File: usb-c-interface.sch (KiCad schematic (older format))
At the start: 60 parts, among them IC3 TPS7A0518PDBVT, J11 12401598E4_2A, J3 12401598E4_2A, J4 12401598E4_2A, U5 TPS25820DSST, U6 FSUSB30MUX, U7 TXB0104RUT, U8 CBTL02043ABQ,115, U9 FT232RQ-REEL

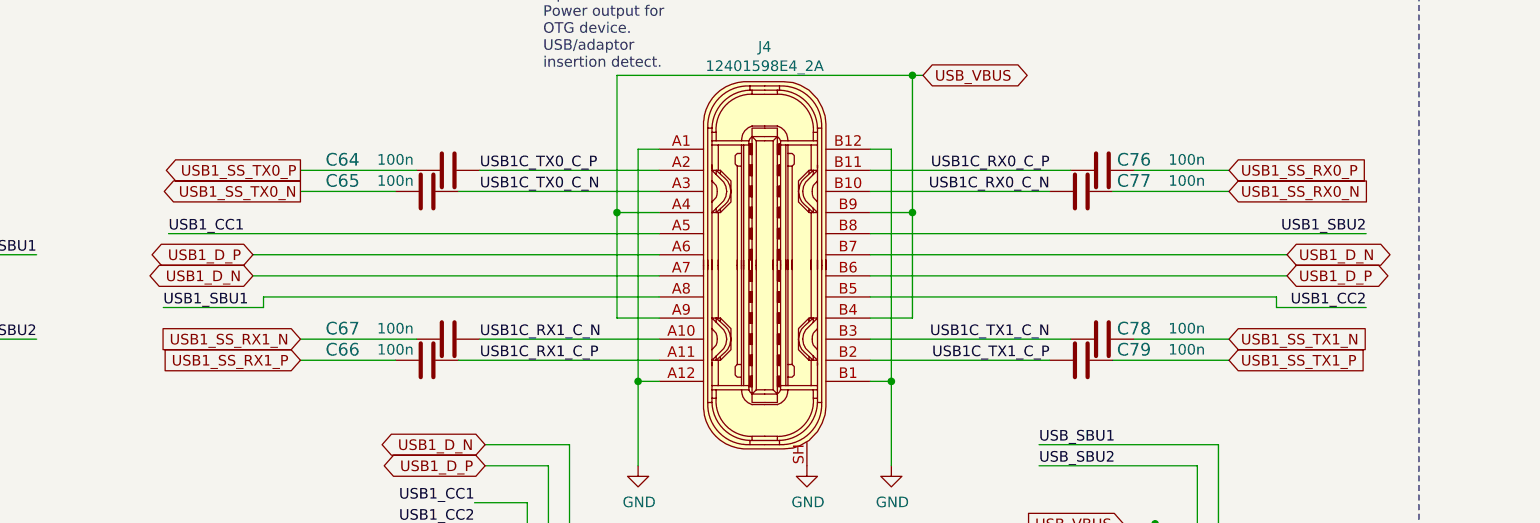
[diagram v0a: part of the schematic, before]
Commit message: Fix connection of CC1 and CC2 signals to som (global and local labels mixed)
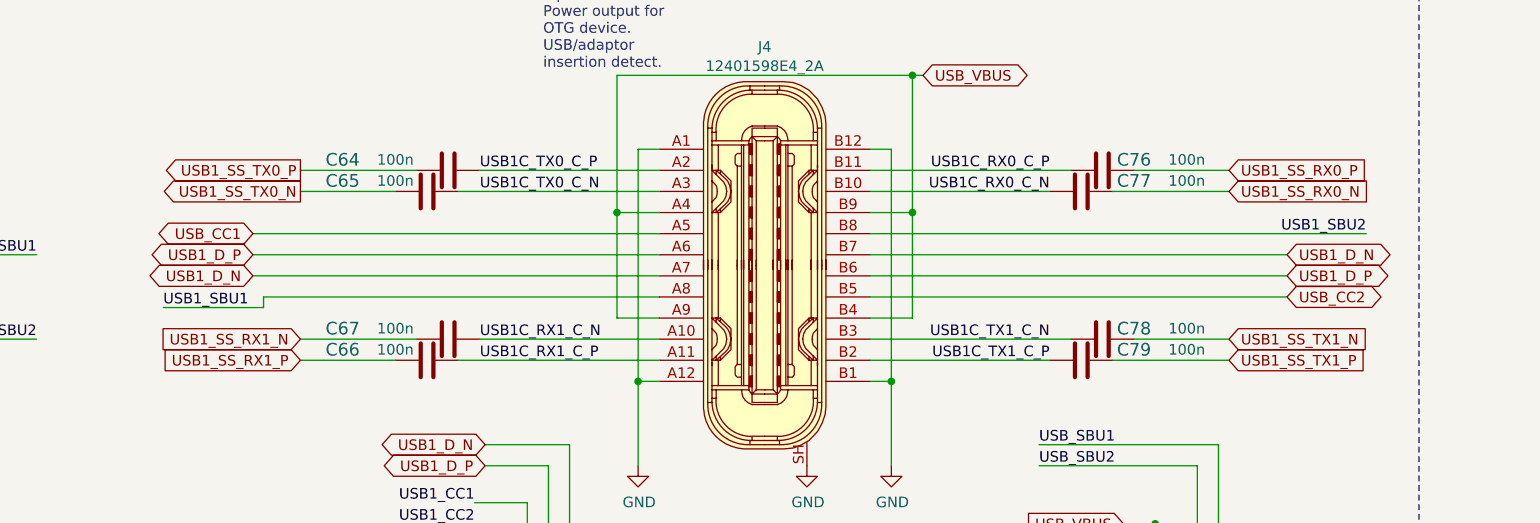
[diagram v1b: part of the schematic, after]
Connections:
- net USB1_CC1: no longer J4.A5
- net USB1_CC2: no longer J4.B5
- new net USB_CC1: J4.A5
- new net USB_CC2: J4.B5
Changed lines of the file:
@@
 Text Label 10950 2225 2    50   ~ 0
 USB1_SBU2
-Text Label 10950 2575 2    50   ~ 0
-USB1_CC2
 Text GLabel 10575 2325 2    50   BiDi ~ 0
 USB1_D_N
@@
 	5250 2575 5725 2575
 Wire Wire Line
-	5275 2225 7600 2225
+	5675 2225 7600 2225
 Wire Wire Line
 	5675 2425 7600 2425
@@
 Text Label 5250 2575 0    50   ~ 0
 USB1_SBU1
-Text Label 5275 2225 0    50   ~ 0
-USB1_CC1
 $Comp
 L sa800u-baseboard-hw:C_100n_0402 C64
@@
 Wire Wire Line
 	8600 2225 10950 2225
-Wire Wire Line
-	10950 2575 10525 2575
-Wire Wire Line
-	10525 2575 10525 2525
-Wire Wire Line
-	10525 2525 8600 2525
 Wire Wire Line
 	9550 2725 8600 2725
@@
 Text GLabel 9350 5750 2    50   Output ~ 0
 USB2_SINK
+Text GLabel 10575 2525 2    50   BiDi ~ 0
+USB_CC2
+Text GLabel 5675 2225 0    50   BiDi ~ 0
+USB_CC1
+Wire Wire Line
+	8600 2525 10575 2525
 $EndSCHEMATC

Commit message: Update labels
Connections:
- net USB_SBU1 is gone; now on net USB1_SBU_P: D9.1 (CH1), D9.10 (CH1)
- net USB_SBU2 is gone; now on net USB1_SBU_P: D9.2 (CH2), D9.9 (CH2)
- net USB1_SBU1 renamed USB1_SBU_N
- net USB1_SBU2 renamed USB1_SBU_P
- net USB_SBU1_2 renamed USB_SBU_NP_P
- net USB_SBU2_1 renamed USB_SBU_NP_N
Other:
- note added: "Note:\nSBU ending with N/P \nto enable routing with \ndifferential tools"
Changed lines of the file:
@@
 $EndComp
 Text Label 10950 2225 2    50   ~ 0
-USB1_SBU2
+USB1_SBU_P
 Text GLabel 10575 2325 2    50   BiDi ~ 0
 USB1_D_N
@@
 Wire Wire Line
 	10050 3600 10050 3775
-Text Label 9400 3325 0    50   ~ 0
-USB_SBU2
 Wire Wire Line
 	9400 3325 10150 3325
@@
 	4175 1575 3900 1575
 Text Label 4650 2325 2    50   ~ 0
-USB1_SBU1
-Text Label 4650 2725 2    50   ~ 0
-USB1_SBU2
-Wire Wire Line
-	4650 2725 4200 2725
+USB1_SBU_N
 Wire Wire Line
 	4650 2325 4200 2325
@@
 	3900 1350 3900 1575
 Connection ~ 3900 1575
-Text Label 3050 2425 2    50   ~ 0
-USB_SBU2_1
-Text Label 3050 2625 2    50   ~ 0
-USB_SBU1_2
+Text Label 3150 2425 2    50   ~ 0
+USB_SBU_NP_N
+Text Label 3150 2625 2    50   ~ 0
+USB_SBU_NP_P
 Text GLabel 2475 2025 0    50   Input ~ 0
 3V3_SYS
@@
 	6350 2825 5900 2825
 Text Label 5250 2575 0    50   ~ 0
-USB1_SBU1
+USB1_SBU_N
 $Comp
 L sa800u-baseboard-hw:C_100n_0402 C64
@@
 	0    1    1    0
 $EndComp
-Text Label 9400 3225 0    50   ~ 0
-USB_SBU1
 $Comp
 L sa800u-baseboard-hw:C_10u_0402 C?
@@
 Wire Wire Line
 	8600 2525 10575 2525
+Text Notes 4100 2650 0    50   ~ 0
+Note:\nSBU ending with N/P \nto enable routing with \ndifferential tools
+Wire Wire Line
+	4650 2725 4200 2725
+Text Label 4650 2725 2    50   ~ 0
+USB1_SBU_P
+Text Label 9400 3225 0    50   ~ 0
+USB1_SBU_P
+Text Label 9400 3325 0    50   ~ 0
+USB1_SBU_P
 $EndSCHEMATC

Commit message: Fix labels
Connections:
- net USB1_CC1 is gone; now on net USB_CC1: D8.4 (CH3), D8.7 (CH3)
- net USB1_CC2 is gone; now on net USB_CC2: D8.5 (CH4), D8.6 (CH4)
- net USB1_SBU_N: now also D9.2 (CH2), D9.9 (CH2)
- net USB1_SBU_P: no longer D9.2 (CH2), D9.9 (CH2)
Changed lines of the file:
@@
 	1    0    0    -1
 $EndComp
-Text Label 6725 3500 2    50   ~ 0
-USB1_CC1
-Text Label 6725 3600 2    50   ~ 0
-USB1_CC2
 Wire Wire Line
 	6725 3600 6875 3600
@@
 USB1_SBU_P
 Text Label 9400 3325 0    50   ~ 0
-USB1_SBU_P
+USB1_SBU_N
+Text GLabel 6725 3500 0    50   BiDi ~ 0
+USB_CC1
+Text GLabel 6725 3600 0    50   BiDi ~ 0
+USB_CC2
 $EndSCHEMATC

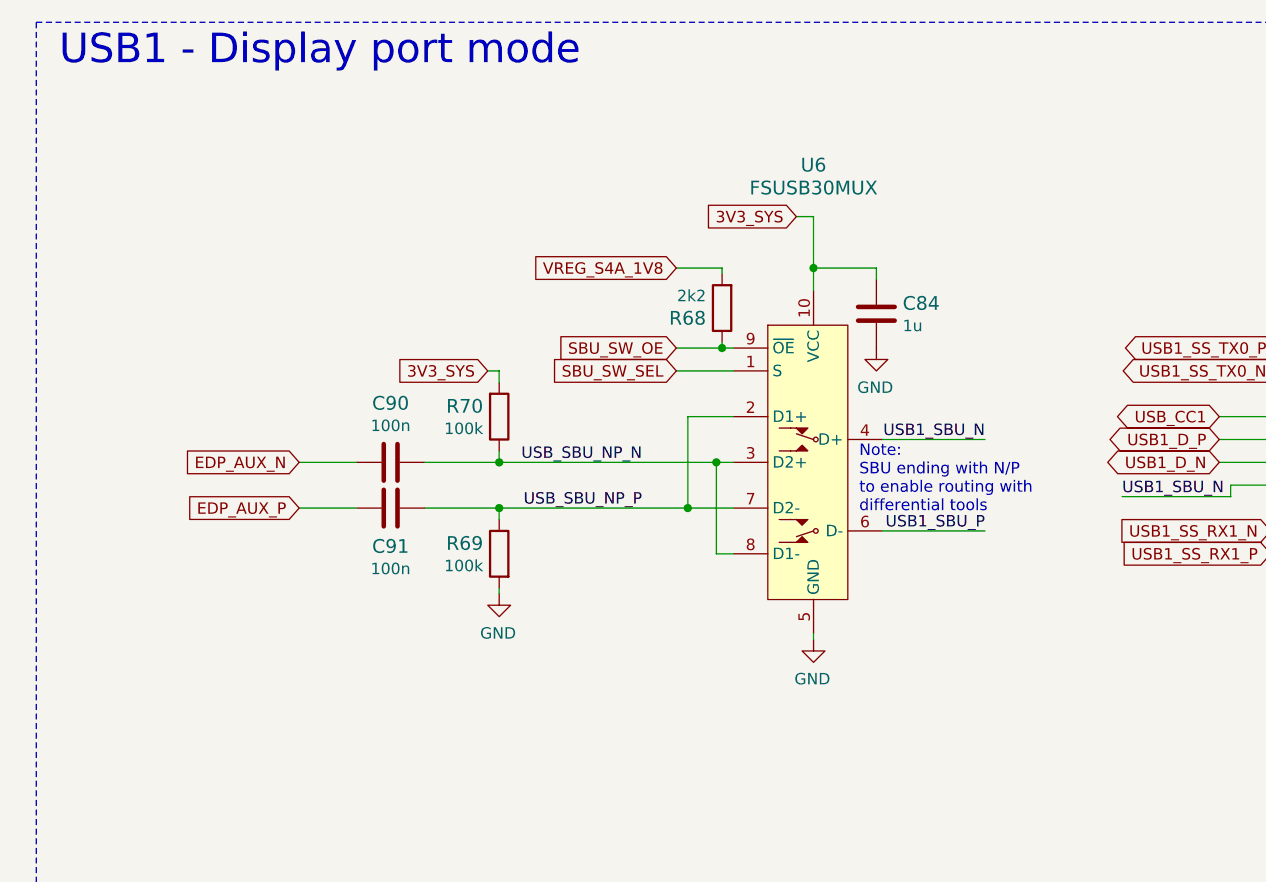
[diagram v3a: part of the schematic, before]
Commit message: Change DP AUX mux
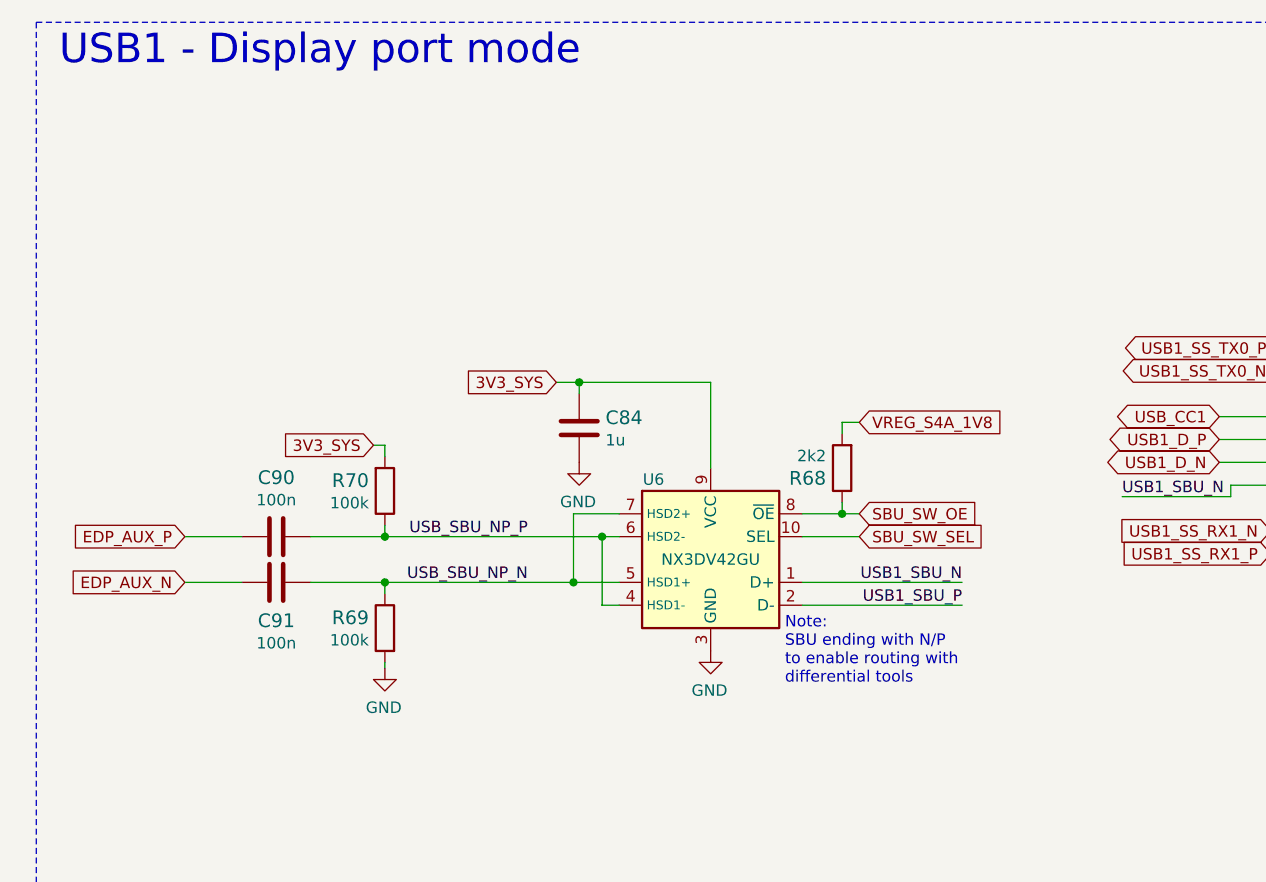
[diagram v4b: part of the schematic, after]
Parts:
- removed U6: FSUSB30MUX, sa800u-baseboard-hw-footprints:MSOP-10_W3mm, symbol sa800u-baseboard-hw:FSUSB30MUX
- added U6: NX3DV42GU, sa800u-baseboard-hw-footprints:XQFN10-1.5x1.9mm, symbol sa800u-baseboard-hw:NX3DV42GU
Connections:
- net 3V3_SYS: now also U6.9 (VCC)
- net EDP_AUX_N: now also C91.1; no longer C90.1
- net EDP_AUX_P: now also C90.1; no longer C91.1
- net GND: now also U6.3 (GND)
- net SBU_SW_OE: now also U6.8 (~OE)
- net SBU_SW_SEL: now also U6.10 (SEL)
- net USB1_SBU_N: now also U6.1 (D+)
- net USB1_SBU_P: now also U6.2 (D-)
- net USB_SBU_NP_N: now also C91.2, R69.1, U6.5 (HSD1+), U6.7 (HSD2+); no longer C90.2, R70.1
- net USB_SBU_NP_P: now also C90.2, R70.1, U6.4 (HSD1-), U6.6 (HSD2-); no longer C91.2, R69.1
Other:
- moved on the sheet: C84, C90, C91, R68, R69, R70

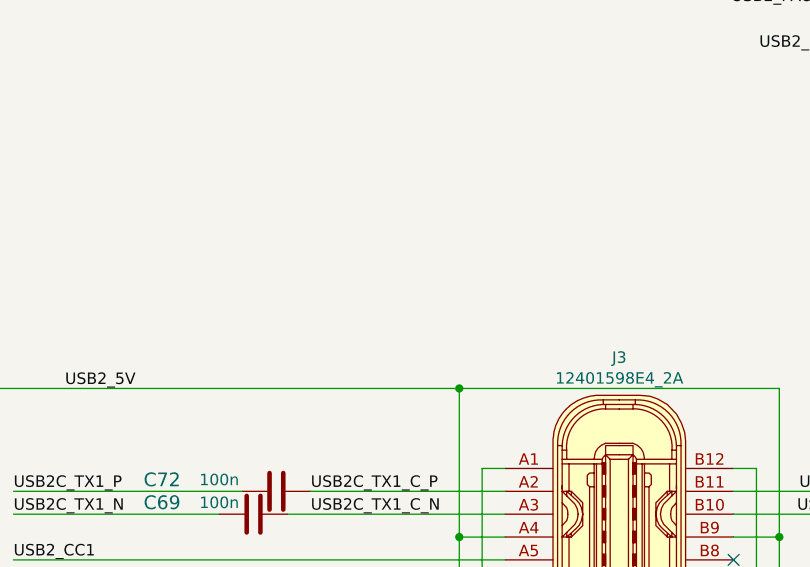
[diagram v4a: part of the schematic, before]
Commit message: Add 47uF caps to USB2C_5V
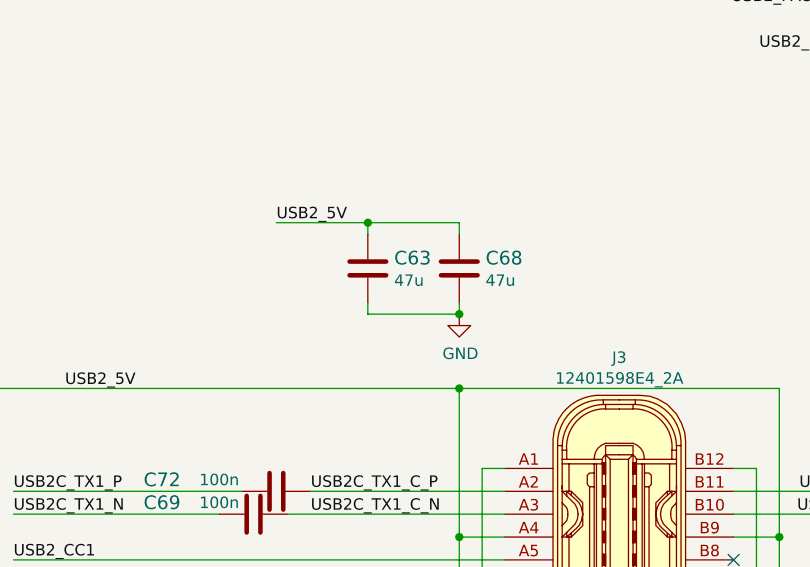
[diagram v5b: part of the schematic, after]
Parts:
- added C63, C68: C_47u_0603, sa800u-baseboard-hw-footprints:0603-cap, symbol sa800u-baseboard-hw:C_47u_0603
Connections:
- net GND: now also C63.2, C68.2
- net USB2_5V: now also C63.1, C68.1
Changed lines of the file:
@@
 Wire Wire Line
 	9625 9575 10325 9575
-Text Label 3000 9950 2    50   ~ 0
-USB2C_TX2_N
-Text Label 3000 9850 2    50   ~ 0
-USB2C_TX2_P
-Text Label 3000 10250 2    50   ~ 0
-USB2C_RX2_N
-Text Label 3000 10150 2    50   ~ 0
-USB2C_RX2_P
-Wire Wire Line
-	2450 9950 3000 9950
-Wire Wire Line
-	2450 9850 3000 9850
-Wire Wire Line
-	2450 10250 3000 10250
-Wire Wire Line
-	2450 10150 3000 10150
-Text Label 3000 9150 2    50   ~ 0
-USB2C_TX1_N
-Text Label 3000 9050 2    50   ~ 0
-USB2C_TX1_P
-Text Label 3000 9450 2    50   ~ 0
-USB2C_RX1_N
-Text Label 3000 9350 2    50   ~ 0
-USB2C_RX1_P
-Wire Wire Line
-	2450 9150 3000 9150
-Wire Wire Line
-	2450 9050 3000 9050
-Wire Wire Line
-	2450 9450 3000 9450
-Wire Wire Line
-	2450 9350 3000 9350
-Text GLabel 1150 9550 0    50   Input ~ 0
-USB2_SS_RX_P
-Text GLabel 1150 9650 0    50   Input ~ 0
-USB2_SS_RX_N
-Text GLabel 1150 9250 0    50   Output ~ 0
-USB2_SS_TX_P
-Text GLabel 1150 9350 0    50   Output ~ 0
-USB2_SS_TX_N
 Wire Wire Line
 	13800 8000 14125 8000
@@
 Wire Wire Line
 	2875 2075 3450 2075
+Text Label 3000 10250 2    50   ~ 0
+USB2C_RX2_N
+Text Label 3000 10150 2    50   ~ 0
+USB2C_RX2_P
+Wire Wire Line
+	2450 10250 3000 10250
+Wire Wire Line
+	2450 10150 3000 10150
+Wire Wire Line
+	2450 9850 3000 9850
+Wire Wire Line
+	2450 9950 3000 9950
+Text Label 3000 9850 2    50   ~ 0
+USB2C_TX2_P
+Text Label 3000 9950 2    50   ~ 0
+USB2C_TX2_N
+Wire Wire Line
+	2450 9050 3000 9050
+Wire Wire Line
+	2450 9150 3000 9150
+Text Label 3000 9050 2    50   ~ 0
+USB2C_TX1_P
+Text Label 3000 9150 2    50   ~ 0
+USB2C_TX1_N
+Wire Wire Line
+	2450 9350 3000 9350
+Wire Wire Line
+	2450 9450 3000 9450
+Text Label 3000 9350 2    50   ~ 0
+USB2C_RX1_P
+Text Label 3000 9450 2    50   ~ 0
+USB2C_RX1_N
+Text GLabel 1150 9350 0    50   Output ~ 0
+USB2_SS_TX_N
+Text GLabel 1150 9250 0    50   Output ~ 0
+USB2_SS_TX_P
+$Comp
+L sa800u-baseboard-hw:C_47u_0603 C?
+U 1 1 62A1CDB5
+P 6000 7100
+AR Path="/628CDA4A/62A1CDB5" Ref="C?"  Part="1"
+AR Path="/61A2F307/62A1CDB5" Ref="C63"  Part="1"
+F 0 "C63" H 6115 7145 60  0000 L CNN
+F 1 "C_47u_0603" H 6000 6950 60  0001 C CNN
+F 2 "sa800u-baseboard-hw-footprints:0603-cap" H 6200 7300 60  0001 L CNN
+F 3 "" H 6000 7100 50  0001 C CNN
+F 4 "MURATA" H 6200 7500 60  0001 L CNN "Manufacturer"
+F 5 "GRM188R60J476ME15D" H 6200 7400 60  0001 L CNN "MPN"
+F 6 "47u" H 6115 7047 50  0000 L CNN "Val"
+	1    6000 7100
+	1    0    0    -1
+$EndComp
+$Comp
+L sa800u-baseboard-hw:C_47u_0603 C?
+U 1 1 62A1CDBE
+P 6400 7100
+AR Path="/628CDA4A/62A1CDBE" Ref="C?"  Part="1"
+AR Path="/61A2F307/62A1CDBE" Ref="C68"  Part="1"
+F 0 "C68" H 6515 7145 60  0000 L CNN
+F 1 "C_47u_0603" H 6400 6950 60  0001 C CNN
+F 2 "sa800u-baseboard-hw-footprints:0603-cap" H 6600 7300 60  0001 L CNN
+F 3 "" H 6400 7100 50  0001 C CNN
+F 4 "MURATA" H 6600 7500 60  0001 L CNN "Manufacturer"
+F 5 "GRM188R60J476ME15D" H 6600 7400 60  0001 L CNN "MPN"
+F 6 "47u" H 6515 7047 50  0000 L CNN "Val"
+	1    6400 7100
+	1    0    0    -1
+$EndComp
+Wire Wire Line
+	6000 6900 6000 6950
+Wire Wire Line
+	5600 6900 6000 6900
+Wire Wire Line
+	6000 6900 6400 6900
+Wire Wire Line
+	6400 6900 6400 6950
+Connection ~ 6000 6900
+Wire Wire Line
+	6400 7250 6400 7300
+Wire Wire Line
+	6400 7300 6000 7300
+Wire Wire Line
+	6000 7300 6000 7250
+$Comp
+L sa800u-baseboard-hw:GND #PWR0248
+U 1 1 62A1CDCC
+P 6400 7300
+AR Path="/61A2F307/62A1CDCC" Ref="#PWR0248"  Part="1"
+AR Path="/628CDA4A/62A1CDCC" Ref="#PWR?"  Part="1"
+F 0 "#PWR0248" H 6400 7050 50  0001 C CNN
+F 1 "GND" H 6405 7127 50  0000 C CNN
+F 2 "" H 6400 7300 50  0001 C CNN
+F 3 "" H 6400 7300 50  0001 C CNN
+	1    6400 7300
+	1    0    0    -1
+$EndComp
+Connection ~ 6400 7300
+Text Label 5600 6900 0    50   ~ 0
+USB2_5V
+Text GLabel 1150 9650 0    50   Input ~ 0
+USB2_SS_RX_N
+Text GLabel 1150 9550 0    50   Input ~ 0
+USB2_SS_RX_P
 $EndSCHEMATC
